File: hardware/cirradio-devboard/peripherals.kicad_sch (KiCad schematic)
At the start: 46 parts, among them J10 USB_A, J11 RJ45_MagJack, J12 USB_Micro_B, J13 U.FL_GPS, J14 Micro_SD, U10 S25FL256S, U11 MTFC8GAKAJCN-8GB, U12 USB3320C-EZK, U13 KSZ9031RNXIA, U14 FT232RQ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

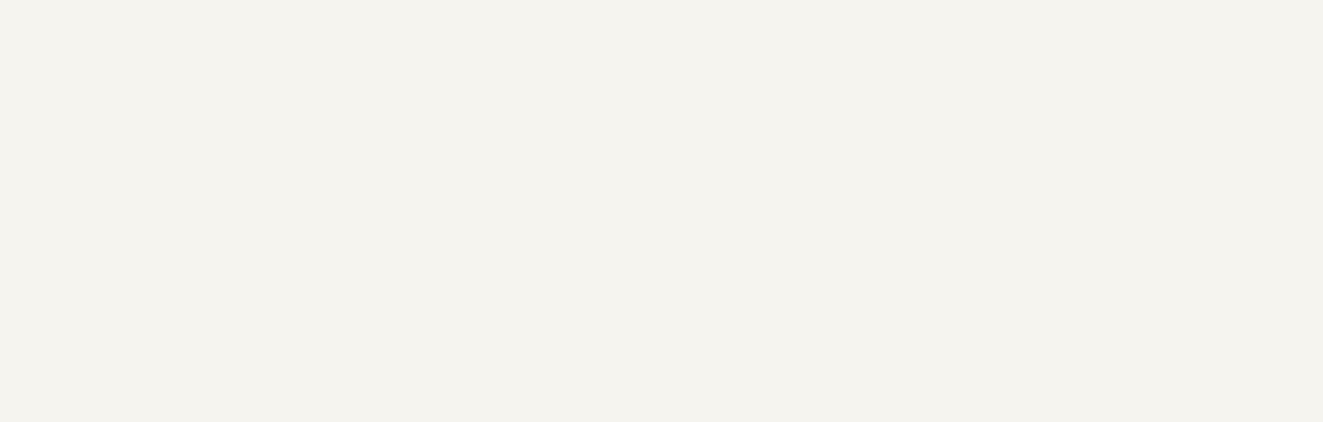
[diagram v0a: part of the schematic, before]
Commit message: update README, add phase 7 plan, refresh peripherals UUIDs
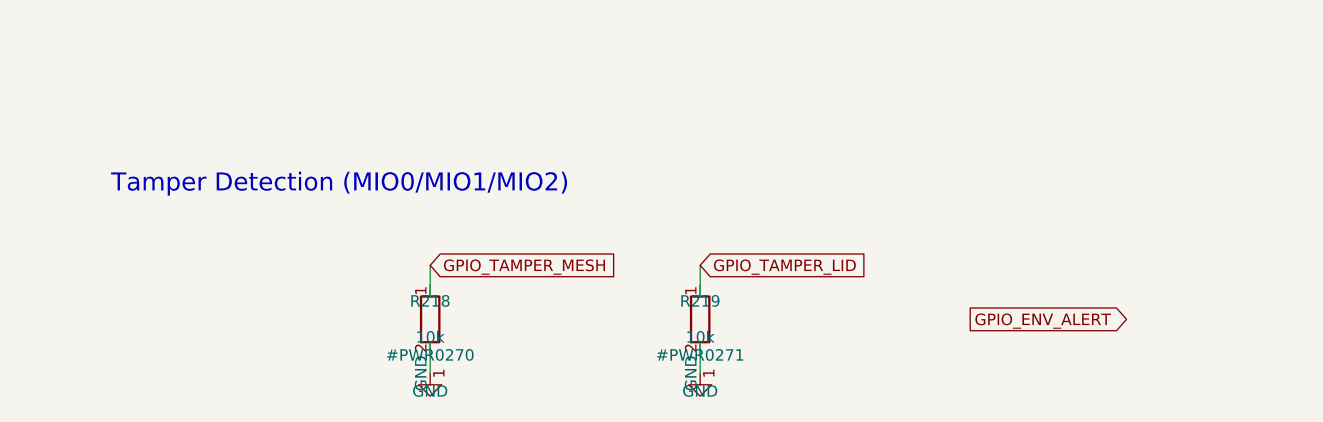
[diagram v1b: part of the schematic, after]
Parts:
- added R218, R219: 10k, symbol Device:R
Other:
- note added: "Tamper Detection (MIO0/MIO1/MIO2)"
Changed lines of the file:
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@@
     )
     (wire (pts (xy 56.19 419.84) (xy 53 419.84)) (stroke (width 0) (type default)))
+    (text "Tamper Detection (MIO0/MIO1/MIO2)" (at 30 495 0) (effects (font (size 2.0 2.0))))
+    (symbol (lib_id "Device:R") (at 40 510 0)
+      (unit 1) (exclude_from_sim no) (in_bom yes) (on_board yes) (dnp no)
+      (property "Reference" "R218" (at 40 508 0) (effects (font (size 1.27 1.27))))
+      (property "Value" "10k" (at 40 512 0) (effects (font (size 1.27 1.27))))
+      (property "Footprint" "" (at 40 510 0) (effects (font (size 1.27 1.27)) hide))
+      (property "Datasheet" "" (at 40 510 0) (effects (font (size 1.27 1.27)) hide))
+      (pin "1")
+      (pin "2")
+    )
+    (wire (pts (xy 40 507.46) (xy 40 504)) (stroke (width 0) (type default)))
+    (global_label "GPIO_TAMPER_MESH" (shape input) (at 40 504 0) (effects (font (size 1.27 1.27)))
+      (property "Intersheetrefs" "${INTERSHEET_REFS}" (at 40 504 0) (effects (font (size 0.5 0.5)) hide))
+    )
+    (wire (pts (xy 40 512.54) (xy 40 516)) (stroke (width 0) (type default)))
+    (symbol (lib_id "power:GND") (at 40 516 0)
+      (unit 1) (exclude_from_sim no) (in_bom yes) (on_board yes) (dnp no)
+      (property "Reference" "#PWR0270" (at 40 514 0) (effects (font (size 1.27 1.27))))
+      (property "Value" "GND" (at 40 518 0) (effects (font (size 1.27 1.27))))
+      (property "Footprint" "" (at 40 516 0) (effects (font (size 1.27 1.27)) hide))
+      (property "Datasheet" "" (at 40 516 0) (effects (font (size 1.27 1.27)) hide))
+      (pin "1")
+    )
+    (symbol (lib_id "Device:R") (at 70 510 0)
+      (unit 1) (exclude_from_sim no) (in_bom yes) (on_board yes) (dnp no)
+      (property "Reference" "R219" (at 70 508 0) (effects (font (size 1.27 1.27))))
+      (property "Value" "10k" (at 70 512 0) (effects (font (size 1.27 1.27))))
+      (property "Footprint" "" (at 70 510 0) (effects (font (size 1.27 1.27)) hide))
+      (property "Datasheet" "" (at 70 510 0) (effects (font (size 1.27 1.27)) hide))
+      (pin "1")
+      (pin "2")
+    )
+    (wire (pts (xy 70 507.46) (xy 70 504)) (stroke (width 0) (type default)))
+    (global_label "GPIO_TAMPER_LID" (shape input) (at 70 504 0) (effects (font (size 1.27 1.27)))
+      (property "Intersheetrefs" "${INTERSHEET_REFS}" (at 70 504 0) (effects (font (size 0.5 0.5)) hide))
+    )
+    (wire (pts (xy 70 512.54) (xy 70 516)) (stroke (width 0) (type default)))
+    (symbol (lib_id "power:GND") (at 70 516 0)
+      (unit 1) (exclude_from_sim no) (in_bom yes) (on_board yes) (dnp no)
+      (property "Reference" "#PWR0271" (at 70 514 0) (effects (font (size 1.27 1.27))))
+      (property "Value" "GND" (at 70 518 0) (effects (font (size 1.27 1.27))))
+      (property "Footprint" "" (at 70 516 0) (effects (font (size 1.27 1.27)) hide))
+      (property "Datasheet" "" (at 70 516 0) (effects (font (size 1.27 1.27)) hide))
+      (pin "1")
+    )
+    (global_label "GPIO_ENV_ALERT" (shape output) (at 100 510 0) (effects (font (size 1.27 1.27)))
+      (property "Intersheetrefs" "${INTERSHEET_REFS}" (at 100 510 0) (effects (font (size 0.5 0.5)) hide))
+    )
 )
